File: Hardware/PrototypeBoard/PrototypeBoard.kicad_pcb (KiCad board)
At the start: 4 copper layers, 160 x 100 mm, 145 parts, among them J1 Conn_01x03, J2 Conn_01x06, J3 ControlSupplyConnector, Q1 Q_NMOS_SGD, Q2 Q_NMOS_SGD, Q3 Q_NMOS_SGD, Q4 Q_NMOS_SGD, Q5 Q_NMOS_SGD, Q6 Q_NMOS_SGD, U1 TLI4970-D025T4, U2 TLI4970-D025T4, U3 TLI4970-D025T4, U4 TLE7185-1E, U5 ADC124S021

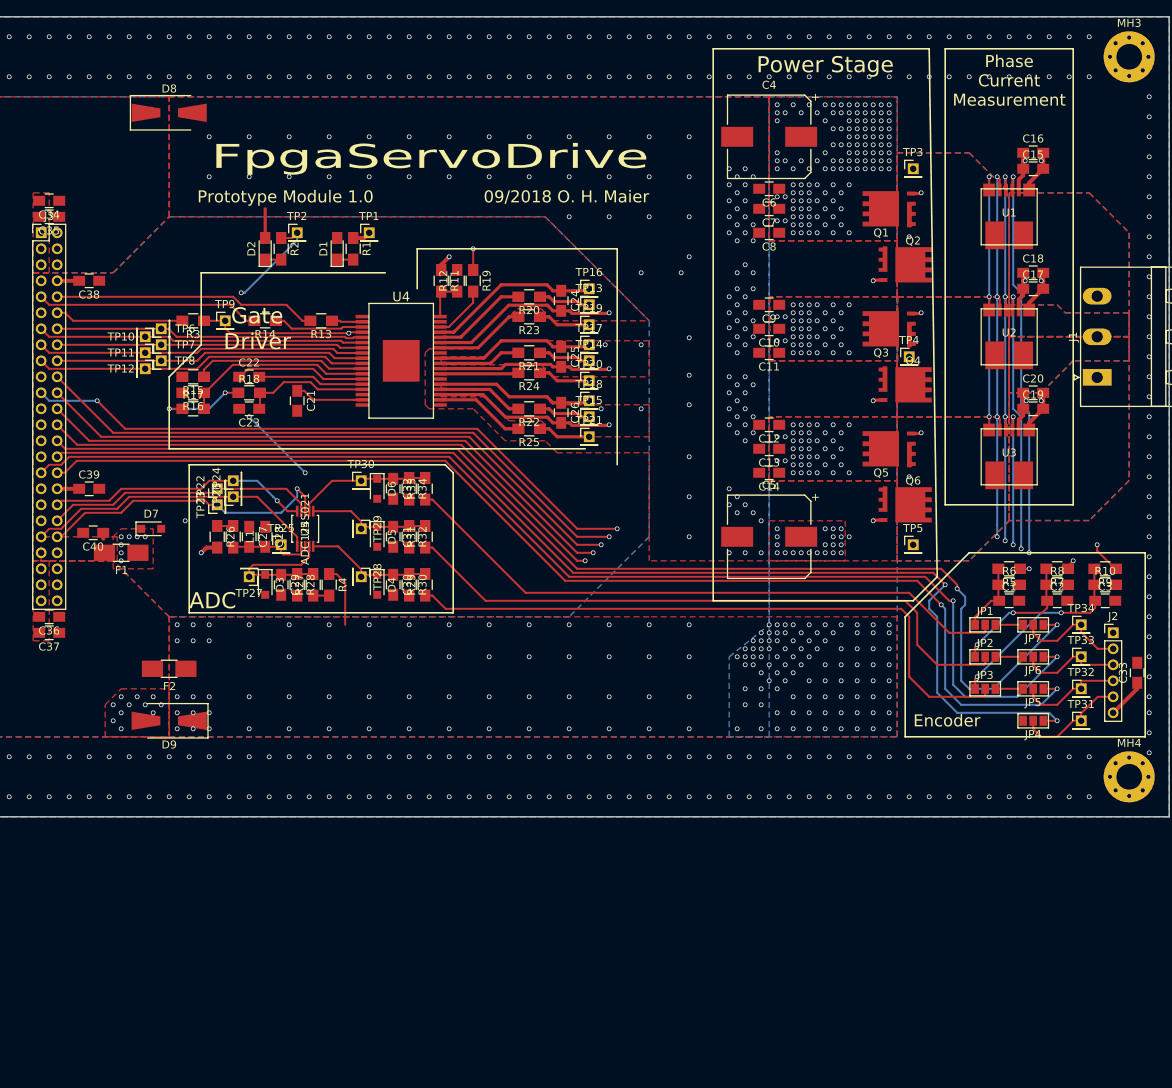
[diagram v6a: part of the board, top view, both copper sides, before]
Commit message: Added LEDs for PWM, SPI communication, Gate Driver Errors and Gate Driver disabled
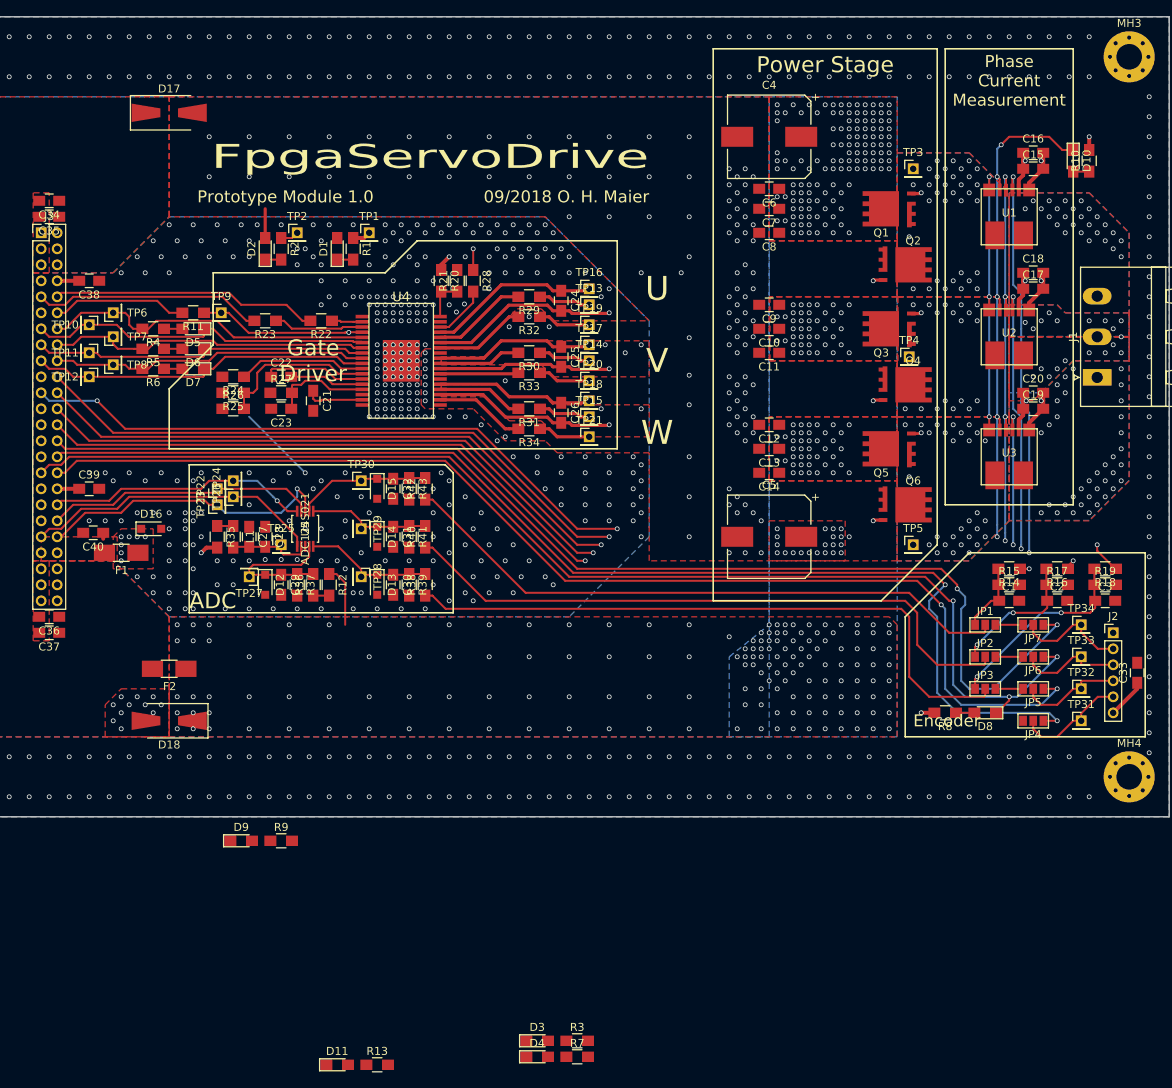
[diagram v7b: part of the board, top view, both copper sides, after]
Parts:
- removed the R15 at (103.0, 85.0)
- removed the R16 at (103.0, 87.0)
- removed the R17 at (103.0, 89.0)
- removed the R18 at (110.0, 87.0)
- added D10: Yellow, LEDs:LED_0805_HandSoldering, F.Cu at (213.0, 58.0)
- added D11: Red, LEDs:LED_0805_HandSoldering, F.Cu at (121.0, 171.0)
- added D3: Red, LEDs:LED_0805_HandSoldering, F.Cu at (146.0, 168.0)
- added D4: Red, LEDs:LED_0805_HandSoldering, F.Cu at (146.0, 170.0)
- added D5: Yellow, LEDs:LED_0805_HandSoldering, F.Cu at (103.0, 79.0)
- added D6: Yellow, LEDs:LED_0805_HandSoldering, F.Cu at (103.0, 81.5)
- added D7: Yellow, LEDs:LED_0805_HandSoldering, F.Cu at (103.0, 84.0)
- added D8: Yellow, LEDs:LED_0805_HandSoldering, F.Cu at (202.0, 127.0)
- added D9: Yellow, LEDs:LED_0805_HandSoldering, F.Cu at (109.0, 143.0)
- added R10: 560, Resistors_SMD:R_0805_HandSoldering, F.Cu at (215.0, 58.0)
- added R13: 220, Resistors_SMD:R_0805_HandSoldering, F.Cu at (126.0, 171.0)
- added R24: 0, Resistors_SMD:R_0805_HandSoldering, F.Cu at (108.0, 85.0)
- added R25: 47k, Resistors_SMD:R_0805_HandSoldering, F.Cu at (108.0, 87.0)
- added R26: 5k, Resistors_SMD:R_0805_HandSoldering, F.Cu at (108.0, 89.0)
- added R27: 4.7, Resistors_SMD:R_0805_HandSoldering, F.Cu at (114.0, 87.0)
- added R3: 220, Resistors_SMD:R_0805_HandSoldering, F.Cu at (151.0, 168.0)
- added R4: 560, Resistors_SMD:R_0805_HandSoldering, F.Cu at (98.0, 79.0)
- added R5: 560, Resistors_SMD:R_0805_HandSoldering, F.Cu at (98.0, 81.5)
- added R6: 560, Resistors_SMD:R_0805_HandSoldering, F.Cu at (98.0, 84.0)
- added R7: 220, Resistors_SMD:R_0805_HandSoldering, F.Cu at (151.0, 170.0)
- added R8: 560, Resistors_SMD:R_0805_HandSoldering, F.Cu at (197.0, 127.0)
- added R9: 560, Resistors_SMD:R_0805_HandSoldering, F.Cu at (114.0, 143.0)
- moved TP10 7.16 mm to (90.0, 78.5)
- moved TP12 7.07 mm to (90.0, 85.0)
- moved TP11 7.00 mm to (90.0, 82.0)
- moved TP6 6.32 mm to (93.0, 77.0)
- moved TP7 6.08 mm to (93.0, 80.0)
- moved TP8 6.02 mm to (93.0, 83.5)
- moved C22 4.00 mm to (114.0, 85.0)
- moved C23 4.00 mm to (114.0, 89.0)
- moved C21 2.00 mm to (118.0, 88.0)
- moved TP9 1.12 mm to (106.5, 77.0)
- moved R11 1.00 mm to (103.0, 77.0)
- renumbered D3 to D12, D4 to D13, D5 to D14, D6 to D15, D7 to D16, D8 to D17, D9 to D18, R3 to R11, R4 to R12, R5 to R14, R6 to R15, R7 to R16, R8 to R17, R9 to R18, R10 to R19, R11 to R20, R12 to R21, R13 to R22, R14 to R23, R19 to R28, R20 to R29, R21 to R30, R22 to R31, R23 to R32, R24 to R33, R25 to R34, R26 to R35, R27 to R36, R28 to R37, R29 to R38, R30 to R39, R31 to R40, R32 to R41, R33 to R42, R34 to R43
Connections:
- C26 pad 2: /MotorModule/CurrentSensing/Power_Phase_W -> /MotorModule/PowerStage/Power_Phase_W
- JP3 pad 2: /MotorModule/Adc/ADC_IN3 -> Net-(JP3-Pad2)
- Q5 pad 1: /MotorModule/CurrentSensing/Power_Phase_W -> /MotorModule/PowerStage/Power_Phase_W
- Q6 pad 3: /MotorModule/CurrentSensing/Power_Phase_W -> /MotorModule/PowerStage/Power_Phase_W
- TP5 pad 1: /MotorModule/CurrentSensing/Power_Phase_W -> /MotorModule/PowerStage/Power_Phase_W
- U4 pad 21: /MotorModule/CurrentSensing/Power_Phase_W -> /MotorModule/PowerStage/Power_Phase_W
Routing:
- net /MotorModule/PowerStage/Power_Phase_W: track 0.00 -> 65.0 mm, vias 0 -> 2
- net /MotorModule/CurrentSensing/Power_Phase_W: track 65.0 -> 0.00 mm, vias 2 -> 28
- net +BATT: track 108.9 -> 69.6 mm, vias 308 -> 389
- net /MainConnector/~CurrentSensSpiCs: track 181.0 -> 195.3 mm, vias 6 -> 7
- net Net-(R24-Pad1): track 22.6 -> 16.0 mm
- net Net-(C22-Pad2): track 13.3 -> 9.27 mm
- net Net-(R25-Pad1): track 23.7 -> 19.9 mm
- net Net-(C22-Pad1): track 16.3 -> 12.8 mm
- net Net-(C23-Pad1): track 15.7 -> 12.4 mm
- net +3V3: track 27.1 -> 30.4 mm
- net /MainConnector/~PwmUH: track 38.7 -> 41.7 mm
- net /MainConnector/~EncoderSpiCs: track 150.2 -> 152.9 mm, vias 2 -> 3
- net /MainConnector/PwmUL: track 40.8 -> 43.5 mm
- net Net-(D8-Pad2): track 0.00 -> 2.30 mm
- net Net-(D7-Pad2): track 0.00 -> 2.30 mm
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- added copper zone on In2.Cu, net GNDPWR
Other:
- board text added: "U"
- board text added: "V"
- board text added: "W"

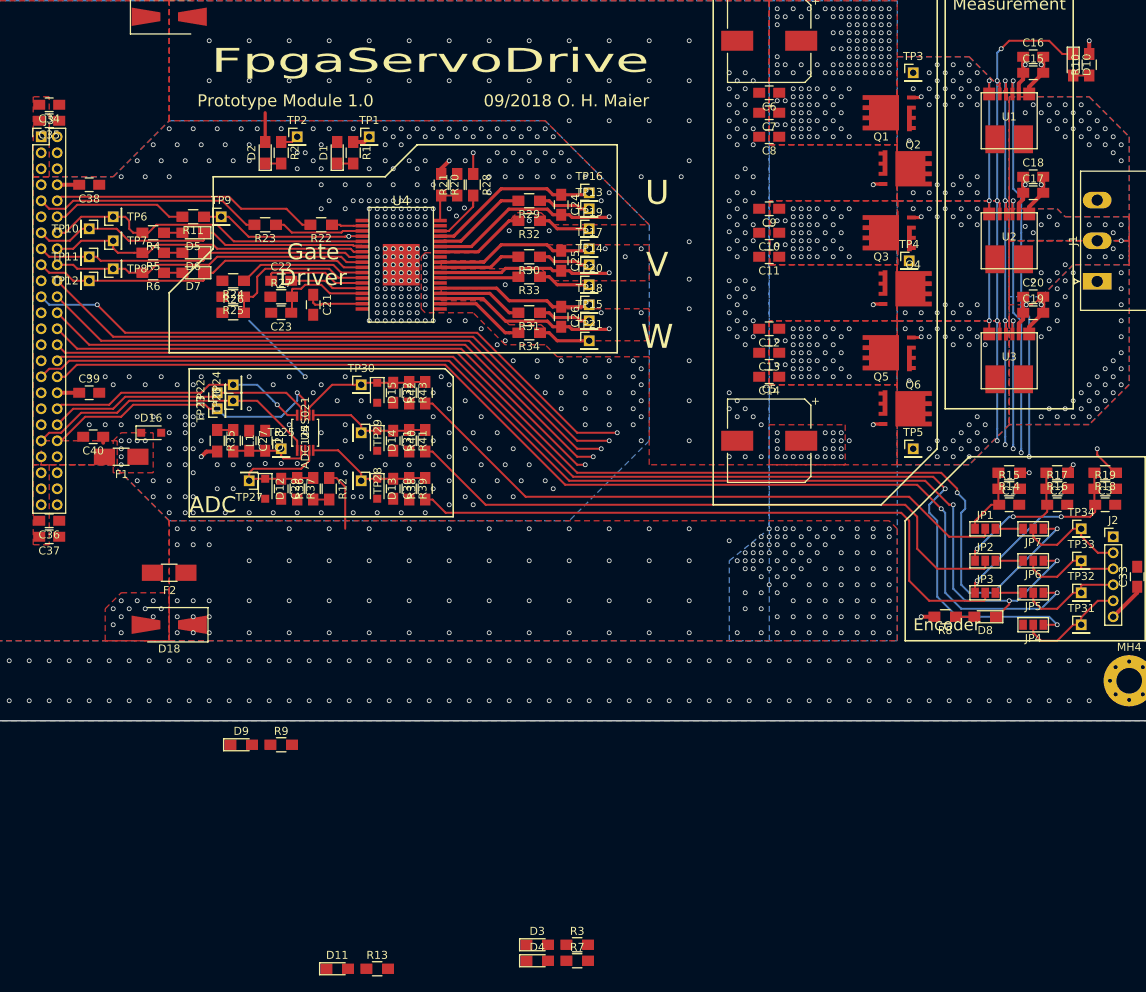
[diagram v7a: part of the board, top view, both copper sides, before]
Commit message: All tracks routed, fixed bug in schematic, smaller test points
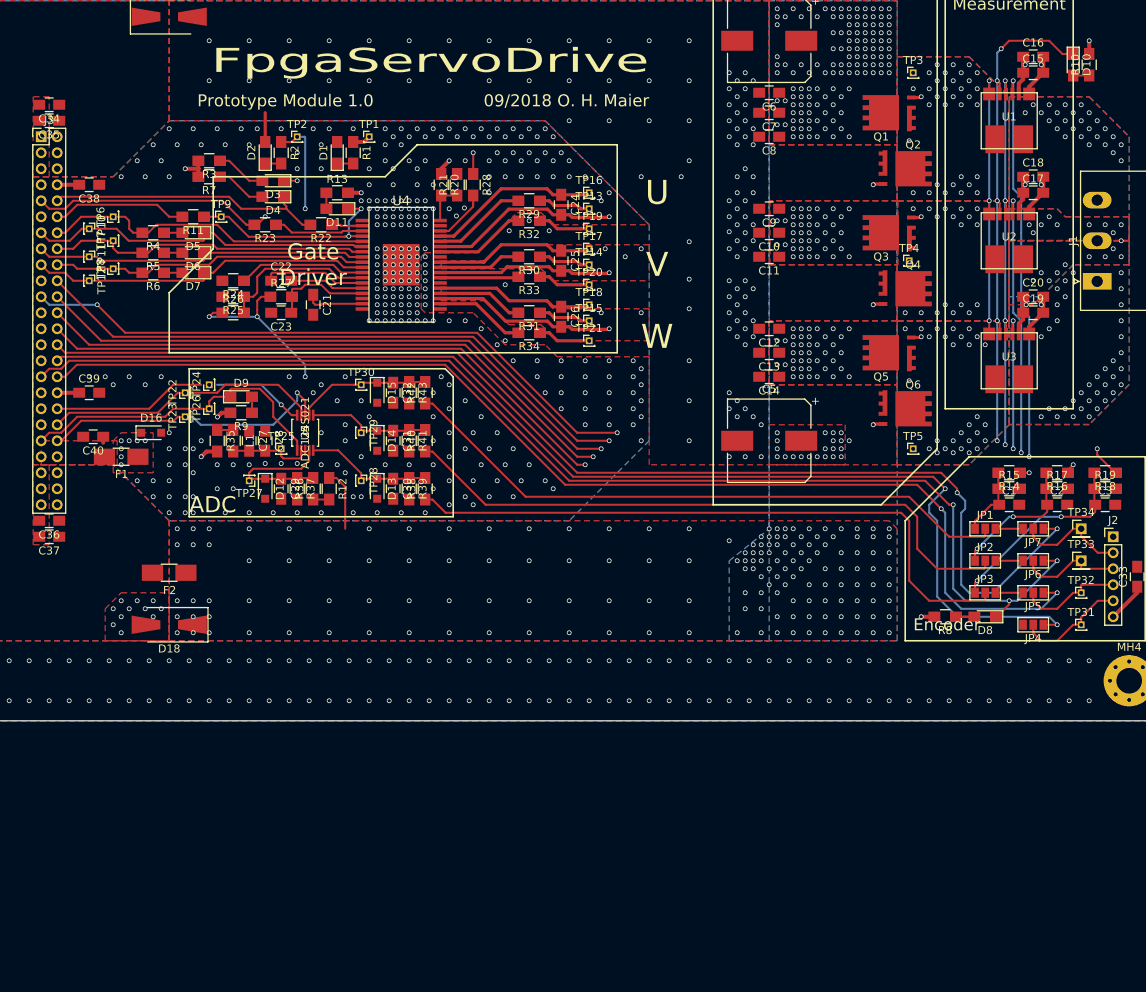
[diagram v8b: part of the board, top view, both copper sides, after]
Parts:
- TP1, TP10, TP11, TP12, TP13, TP14, TP15, TP16, TP17, TP18, TP19, TP2, TP20, TP21, TP22, TP23, TP24, TP25, TP26, TP27, TP28, TP29, TP3, TP30, TP31, TP32, TP4, TP5, TP6, TP7, TP8, TP9: footprint Pin_Headers:Pin_Header_Straight_1x01_Pitch2.00mm -> Pin_Headers:Pin_Header_Straight_1x01_Pitch1.00mm
- moved R3 108.3 mm to (105.0, 70.0), turned to 180 degrees
- moved R7 108.3 mm to (105.0, 72.0), turned to 180 degrees
- moved D3 101.0 mm to (113.0, 72.5), turned to 180 degrees
- moved D4 101.0 mm to (113.0, 74.5), turned to 180 degrees
- moved R13 97.1 mm to (121.0, 74.0)
- moved D11 95.0 mm to (121.0, 76.0), turned to 180 degrees
- moved D9 43.5 mm to (109.0, 99.5)
- moved R9 41.8 mm to (109.0, 101.5), turned to 180 degrees
- moved TP23 4.12 mm to (102.0, 102.0)
- moved TP22 4.00 mm to (102.0, 99.0)
- moved TP26 3.16 mm to (105.0, 101.0)
- moved TP24 3.00 mm to (105.0, 98.0)
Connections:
- C26 pad 2: /MotorModule/PowerStage/Power_Phase_W -> /MotorModule/CurrentSensing/Power_Phase_W
- JP3 pad 2: Net-(JP3-Pad2) -> /MotorModule/Adc/ADC_IN3
- Q5 pad 1: /MotorModule/PowerStage/Power_Phase_W -> /MotorModule/CurrentSensing/Power_Phase_W
- Q6 pad 3: /MotorModule/PowerStage/Power_Phase_W -> /MotorModule/CurrentSensing/Power_Phase_W
- TP5 pad 1: /MotorModule/PowerStage/Power_Phase_W -> /MotorModule/CurrentSensing/Power_Phase_W
- U4 pad 21: /MotorModule/PowerStage/Power_Phase_W -> /MotorModule/CurrentSensing/Power_Phase_W
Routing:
- net /MotorModule/PowerStage/Power_Phase_W: track 65.0 -> 0.00 mm, vias 2 -> 0
- net /MotorModule/CurrentSensing/Power_Phase_W: track 0.00 -> 65.0 mm, vias 28 -> 30
- net +BATT: track 69.6 -> 108.2 mm, vias 389 -> 392
- net /MainConnector/~GateDriverErr1: track 28.7 -> 38.3 mm, vias 0 -> 2
- net +3V3: track 30.4 -> 37.5 mm, vias 14 -> 17
- net Net-(D4-Pad2): track 0.00 -> 6.34 mm
- net Net-(D3-Pad2): track 0.00 -> 6.34 mm
- net /MotorModule/GateDriver/Logic_GD_ENA: track 137.7 -> 143.5 mm, vias 4 -> 5
- net /MainConnector/~AdcSpiCs: track 37.3 -> 40.7 mm
- net Net-(D9-Pad2): track 0.00 -> 2.00 mm
- net Net-(D11-Pad2): track 0.00 -> 2.00 mm
- net /MainConnector/AdcSpiSclk: track 32.8 -> 30.8 mm
- net /MainConnector/~GateDriverErr2: track 33.3 -> 34.9 mm
- net /MainConnector/AdcSpiMiso: track 33.9 -> 34.7 mm
- net GND: vias 635 -> 604
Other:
- net class Default: clearance 0.2 -> 0.165
- rule trace_clearance: 0.2 -> 0.165
